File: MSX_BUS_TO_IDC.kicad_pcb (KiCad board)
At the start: 2 copper layers, 103 x 66 mm, 87 parts, among them J1 DE1 GPIO, J10 Conn_01x01, J11 Conn_01x01, J12 Conn_01x01, J13 Conn_01x01, J14 Conn_01x01, J15 Conn_01x01, J16 Conn_01x01, J17 Conn_01x01, J18 Conn_01x01, J19 Conn_01x01, J2 Conn_02x01, J20 Conn_01x01, J21 Conn_01x01, J22 Conn_01x01, J23 Conn_01x01, J24 Conn_01x01, J25 Conn_01x01, J26 Conn_01x01, J27 Conn_01x01, J28 Conn_01x01, J29 Conn_01x01, J3 Conn_02x01, J30 Conn_01x01, J31 Conn_01x01, J32 Conn_01x01, J33 Conn_01x01, J34 Conn_01x01, J35 Conn_01x01, J36 Conn_01x01, J37 Conn_01x01, J38 Conn_01x01, J39 Conn_01x01, J4 Conn_01x01, J40 Conn_01x01, J41 Conn_01x01, J42 Conn_01x01, J43 Conn_01x01, J44 Conn_01x01, J45 Conn_01x01, J46 Conn_01x01, J47 Conn_01x01, J48 Conn_01x01, J49 Conn_01x01, J5 Conn_01x01, J50 Conn_01x01, J51 Conn_01x01, J52 Conn_01x01, J53 Conn_01x01, J54 Conn_01x01, J55 Conn_01x01, J56 Conn_01x01, J57 Conn_01x01, J58 Conn_01x01, J59 Conn_01x01, J6 Conn_01x01, J60 Conn_01x01, J61 Conn_01x01, J62 Conn_01x01, J63 Conn_01x01, J64 Conn_01x01, J65 Conn_01x01, J66 Conn_01x01, J67 Conn_01x01, J68 Conn_01x01, J69 Conn_01x01, J7 Conn_01x01, J70 Conn_01x01, J71 Conn_01x01, J72 Conn_01x01, J73 Conn_01x01, J74 Conn_01x01, J8 Conn_01x01, J9 Conn_01x01

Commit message: Fabrication files added
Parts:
- moved G*** 2.45 mm to (105.0, 66.8)
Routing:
- net GND: track 183.7 -> 173.5 mm, vias 1 -> 0
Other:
- board text added: "Attention: Must not be used with Real MSX. They have 5V bus, and might damage the DE1 board. Safe to use with FPGA MSX Clones (Zemmix / 1ChipMSX) because they already operate at 3.3V."
- board text added: "MSX BUS to IDC (Use Only with FPGA Clones)"
- board text added: "MSX BUS to IDC interface. Designed for Alrera DE1 Development Board"
- board text added: "RCC @ 2022"
- board text added: "V1.0"
- board text added: "https://github.com/costarc/MSX_BUS_TO_IDC"
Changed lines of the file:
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@@
   )
   (footprint "LOGO" (layer "F.Cu")
-    (at 103.8 64.7)
+    (at 104.995192 66.836538)
     (attr board_only exclude_from_pos_files exclude_from_bom)
-    (fp_text reference "G***" (at 0 0) (layer "F.SilkS")
+    (fp_text reference "G***" (at 0 0) (layer "F.SilkS") hide
       (effects (font (size 1.524 1.524) (thickness 0.3)))
     )
@@
       (net 111 "unconnected-(J65-Pad1)") (pinfunction "Pin_1") (pintype "passive"))
   )
+  (gr_text "Attention:\nMust not be used with Real MSX.\nThey have 5V bus, and might damage the DE1 board.\nSafe to use with FPGA MSX Clones (Zemmix / 1ChipMSX) \nbecause they already operate at 3.3V." (at 105 60) (layer "B.SilkS")
+    (effects (font (size 1 1) (thickness 0.15)) (justify mirror))
+  )
+  (gr_text "MSX BUS to IDC interface.\nDesigned for Alrera DE1 Development Board" (at 105 37.5) (layer "B.SilkS")
+    (effects (font (size 1 1) (thickness 0.15)) (justify mirror))
+  )
   (gr_text "D1" (at 60.25 45.75) (layer "F.SilkS")
     (effects (font (size 0.6 0.6) (thickness 0.11)))
@@
   (gr_text "D5" (at 82.25 39.5) (layer "F.SilkS")
     (effects (font (size 0.6 0.6) (thickness 0.11)))
+  )
+  (gr_text "https://github.com/costarc/MSX_BUS_TO_IDC" (at 104.418803 56.633903) (layer "F.SilkS")
+    (effects (font (size 1 1) (thickness 0.15)))
   )
   (gr_text "A11" (at 108 39.5) (layer "F.SilkS")
@@
     (effects (font (size 0.6 0.6) (thickness 0.11)))
   )
+  (gr_text "V1.0" (at 152.070512 81.157051) (layer "F.SilkS")
+    (effects (font (size 1 1) (thickness 0.15)))
+  )
+  (gr_text "MSX BUS to IDC\n(Use Only with FPGA Clones)" (at 64.89423 76.427884) (layer "F.SilkS")
+    (effects (font (size 1 1) (thickness 0.15)) (justify left))
+  )
   (gr_text "GND" (at 115 39.5) (layer "F.SilkS")
     (effects (font (size 0.6 0.6) (thickness 0.11)))
@@
   (gr_text "D0" (at 60.25 47.75) (layer "F.SilkS")
     (effects (font (size 0.6 0.6) (thickness 0.11)))
+  )
+  (gr_text "RCC @ 2022" (at 70 80) (layer "F.SilkS")
+    (effects (font (size 1 1) (thickness 0.15)))
   )
   (gr_text "A5" (at 89.75 39.5) (layer "F.SilkS")
@@
   (segment (start 111.395 49.645) (end 111.395 31.105) (width 0.35) (layer "F.Cu") (net 2))
   (segment (start 124.042025 62.292025) (end 111.395 49.645) (width 0.35) (layer "F.Cu") (net 2))
-  (via (at 92.2 71.5) (size 0.8) (drill 0.4) (layers "F.Cu" "B.Cu") (free) (net 3))
-  (segment (start 92.2 71.5) (end 91.297655 72.402345) (width 1) (layer "B.Cu") (net 3))
-  (segment (start 88.482025 77.417975) (end 88.482025 80.232025) (width 1) (layer "B.Cu") (net 3))
   (segment (start 115.16 33.0375) (end 113.935 31.8125) (width 0.35) (layer "B.Cu") (net 3))
   (segment (start 88.7375 36.6) (end 92.3 33.0375) (width 1) (layer "B.Cu") (net 3))
@@
   (segment (start 149.4 33.29) (end 144.75 33.29) (width 1) (layer "B.Cu") (net 3))
   (segment (start 57.5 59.8) (end 57.5 38.75) (width 1) (layer "B.Cu") (net 3))
-  (segment (start 91.297655 72.402345) (end 91.297655 74.602345) (width 1) (layer "B.Cu") (net 3))
   (segment (start 88.482025 87.014405) (end 88.482025 80.232025) (width 1) (layer "B.Cu") (net 3))
   (segment (start 59.65 36.6) (end 88.7375 36.6) (width 1) (layer "B.Cu") (net 3))
@@
   (segment (start 75.45 77.75) (end 57.5 59.8) (width 1) (layer "B.Cu") (net 3))
   (segment (start 143.04 35) (end 117.1225 35) (width 1) (layer "B.Cu") (net 3))
-  (segment (start 91.297655 74.602345) (end 88.482025 77.417975) (width 1) (layer "B.Cu") (net 3))
   (segment (start 113.935 31.8125) (end 93.525 31.8125) (width 0.35) (layer "B.Cu") (net 3))
   (segment (start 144.75 33.29) (end 143.04 35) (width 1) (layer "B.Cu") (net 3))

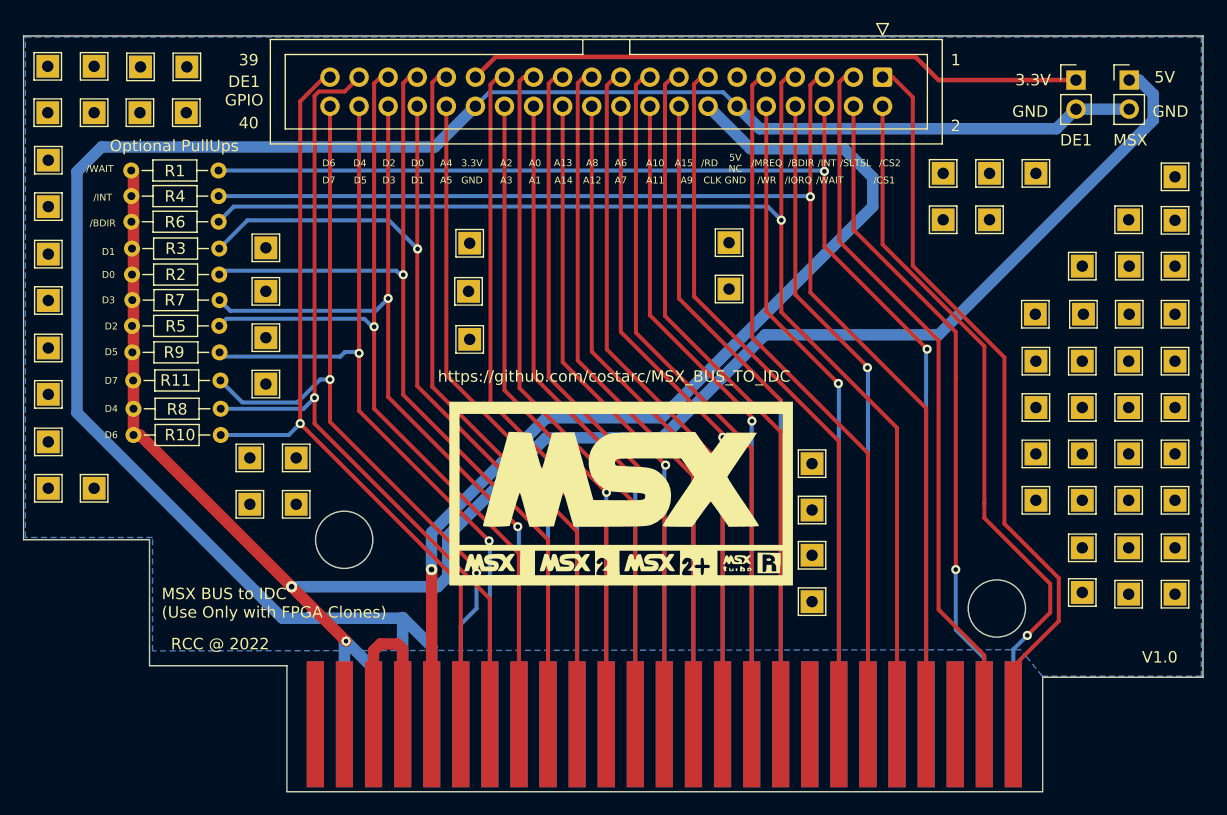
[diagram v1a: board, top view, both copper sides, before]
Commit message: Adjusted footprints for resistors
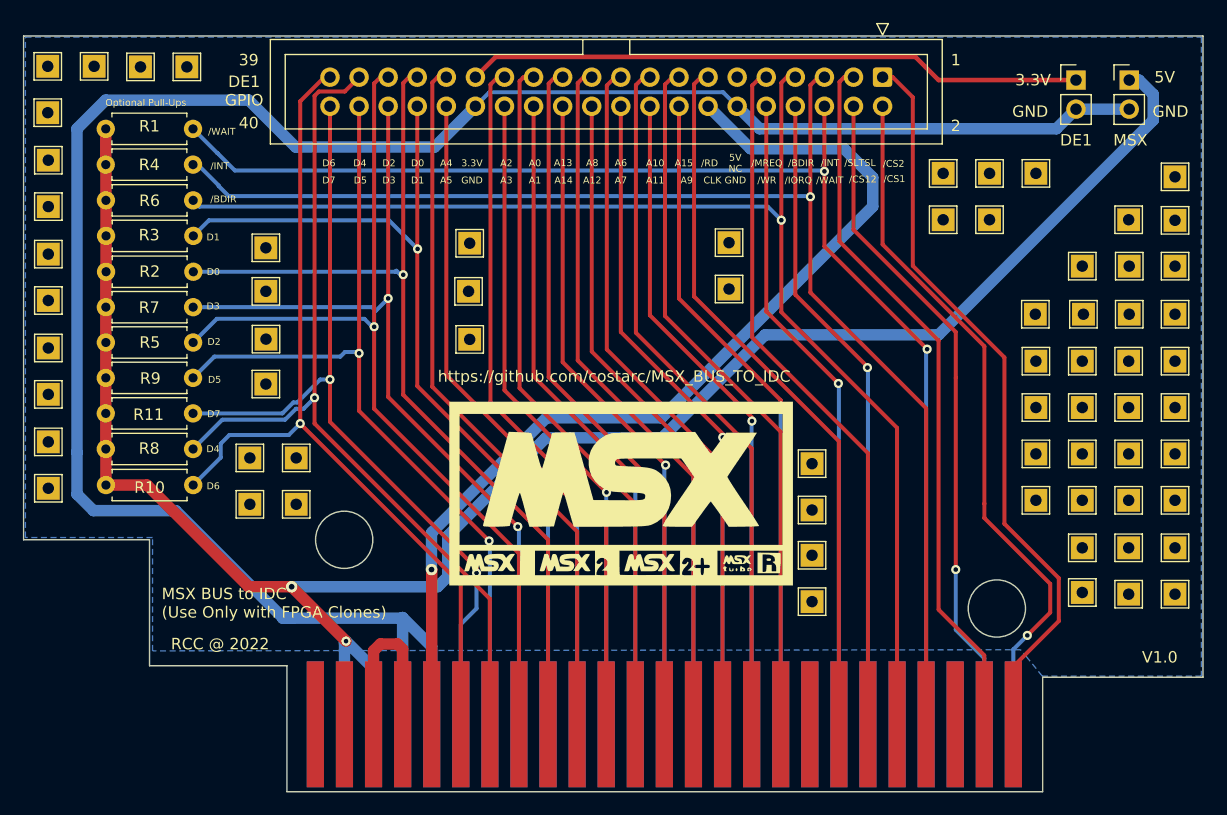
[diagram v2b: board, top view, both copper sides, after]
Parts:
- removed J71, J72, J73, J74: Conn_01x01, TestPoint:TestPoint_THTPad_2.0x2.0mm_Drill1.0mm
- R1, R10, R11, R2, R3, R4, R5, R6, R7, R8, R9: footprint Resistor_THT:R_Axial_DIN0204_L3.6mm_D1.6mm_P7.62mm_Horizontal -> Resistor_THT:R_Axial_DIN0207_L6.3mm_D2.5mm_P7.62mm_Horizontal
- moved J42 24.8 mm to (74.0, 53.4)
- moved R10 4.99 mm to (60.0, 66.1)
- moved R8 4.26 mm to (60.0, 63.0)
- moved R1 4.26 mm to (60.0, 35.0)
- moved R11 3.74 mm to (60.0, 59.9)
- moved R4 3.54 mm to (60.0, 38.1)
- moved R9 3.21 mm to (60.0, 56.8)
- moved R6 2.90 mm to (60.0, 41.3)
- moved R5 2.70 mm to (60.0, 53.7)
- moved R3 2.52 mm to (60.0, 44.4)
- moved R7 2.39 mm to (60.0, 50.6)
- moved R2 2.28 mm to (60.0, 47.5)
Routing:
- net GND: track 173.5 -> 184.1 mm
- net 5V: track 163.6 -> 172.2 mm
- net D6: track 71.3 -> 76.2 mm
- net D4: track 74.4 -> 78.3 mm
- net /WAIT: track 111.2 -> 114.9 mm
- net /INT: track 113.2 -> 116.6 mm
- net D5: track 71.6 -> 74.5 mm
- net D2: track 76.5 -> 79.4 mm
- net D0: track 78.8 -> 81.0 mm
- net D3: track 74.5 -> 76.6 mm
- net D7: track 71.5 -> 73.5 mm
- net /BUSDIR: track 111.8 -> 113.7 mm
- net D1: track 78.6 -> 80.4 mm
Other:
- board text added: "/CS12"
- board text added: "Optional Pull-Ups"
- board text removed: "Optional PullUps"
